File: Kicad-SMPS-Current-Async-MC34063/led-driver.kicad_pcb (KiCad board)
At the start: 2 copper layers, 40 x 25 mm, 16 parts, among them J1 Input 12V-30V, J2 Output, U1 MC34063, U2 LM321

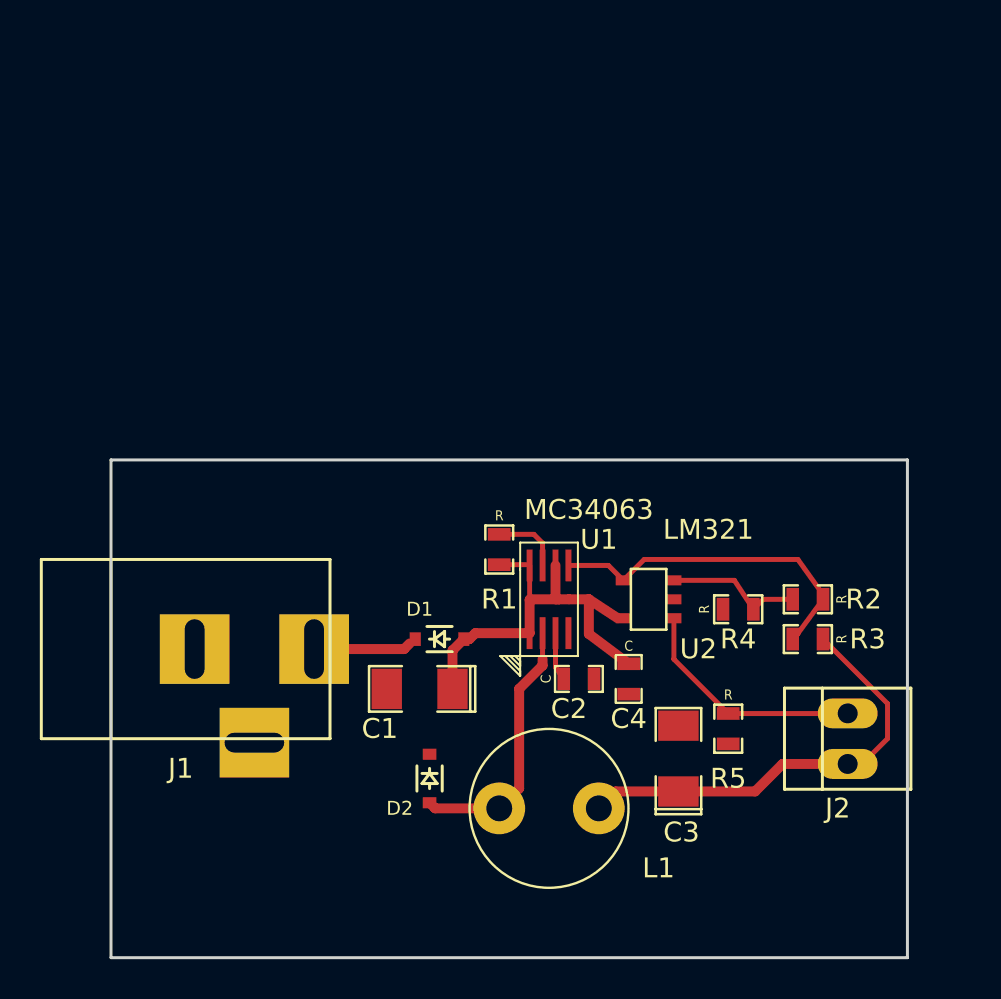
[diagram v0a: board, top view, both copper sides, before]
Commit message: Rebuild PCB to correct errors and generate group of eight circuits.
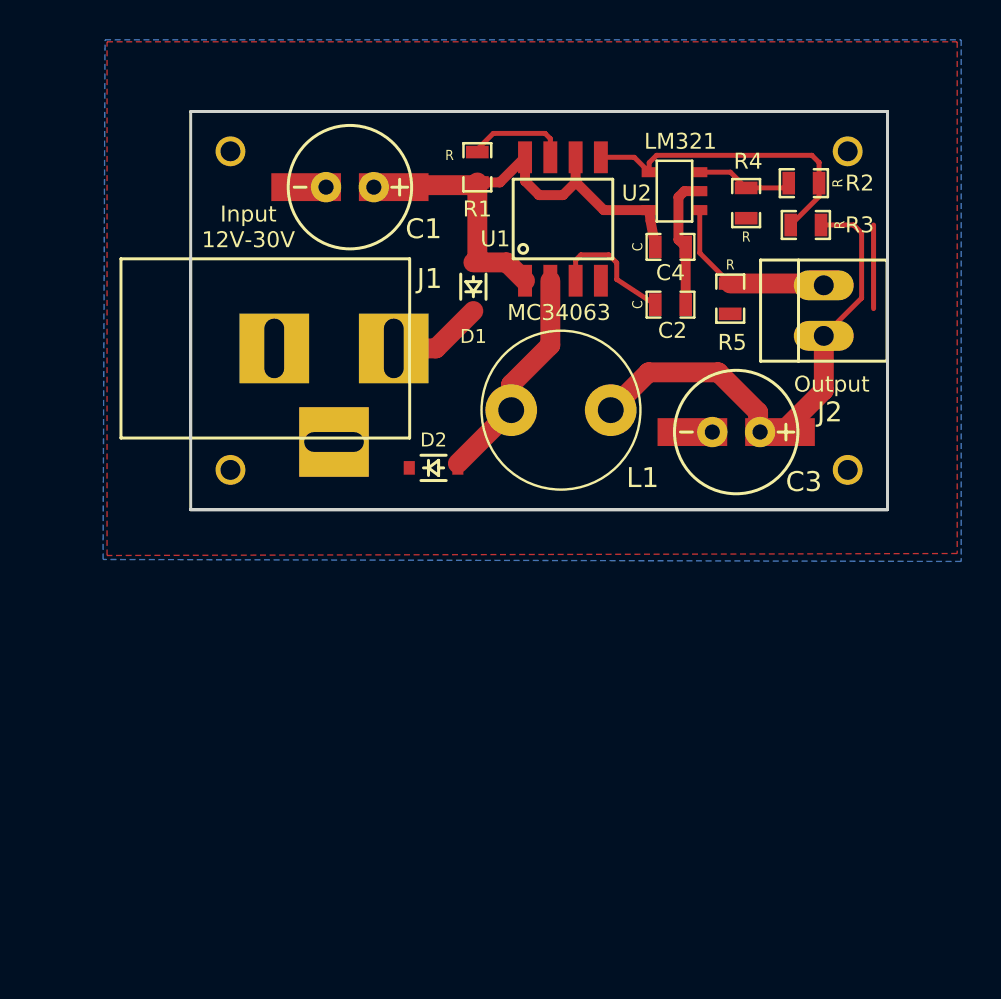
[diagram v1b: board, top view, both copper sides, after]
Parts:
- added J3: Conn_01x01, smps-current-source:THROUGHVIA, F.Cu at (157.0, 109.5)
- added J3: Conn_01x01, smps-current-source:THROUGHVIA, F.Cu at (126.0, 109.5)
- added J3: Conn_01x01, smps-current-source:THROUGHVIA, F.Cu at (126.0, 125.5)
- added J3: Conn_01x01, smps-current-source:THROUGHVIA, F.Cu at (157.0, 125.5)
- C1, C3: footprint smps-current-source:SM1206POL -> smps-current-source:RADIAL_TABBED_2.5mm_6.3mm
- U1: footprint smps-current-source:DCT(R-PDSO-G8) -> smps-current-source:SOIC_08_4.0mm_5.0mm_1.27mm
- moved C1 25.4 mm to (132.0, 111.3), turned to 0 degrees
- moved C4 21.8 mm to (148.1, 114.3), turned to 0 degrees
- moved R5 21.6 mm to (151.1, 116.9)
- moved J2 21.5 mm to (155.8, 117.5)
- moved R2 20.9 mm to (154.8, 111.1)
- moved R3 20.8 mm to (154.9, 113.2)
- moved U2 20.5 mm to (148.3, 111.5)
- moved R4 20.4 mm to (151.9, 112.1), turned to 90 degrees
- moved L1 20.0 mm to (140.1, 122.5)
- moved C2 19.4 mm to (148.1, 117.2)
- moved R1 19.2 mm to (138.4, 110.3)
- moved U1 19.1 mm to (142.7, 112.9)
- moved D1 17.8 mm to (138.2, 116.3), turned to 270 degrees
- moved C3 16.7 mm to (151.4, 123.6), turned to 0 degrees
- moved J1 15.6 mm to (128.0, 119.4)
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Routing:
- net Earth: track 0.00 -> 6.74 mm
- net /Vcc: track 22.2 -> 27.1 mm
- net (no net): track 0.00 -> 4.20 mm
- net Net-(C2-Pad1): track 2.43 -> 6.52 mm
- net Net-(C3-Pad1): track 21.8 -> 25.5 mm
- net Net-(J2-Pad2): track 11.9 -> 9.06 mm
- net Net-(D2-Pad1): track 13.6 -> 11.3 mm
- net Net-(R2-Pad2): track 6.96 -> 4.89 mm
- net Net-(R1-Pad1): track 3.48 -> 5.18 mm
- net Net-(R2-Pad1): track 17.0 -> 15.8 mm
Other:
- board size 40 x 25 mm -> 35 x 20 mm
- board text added: "Input 12V-30V"
- board text added: "Output"

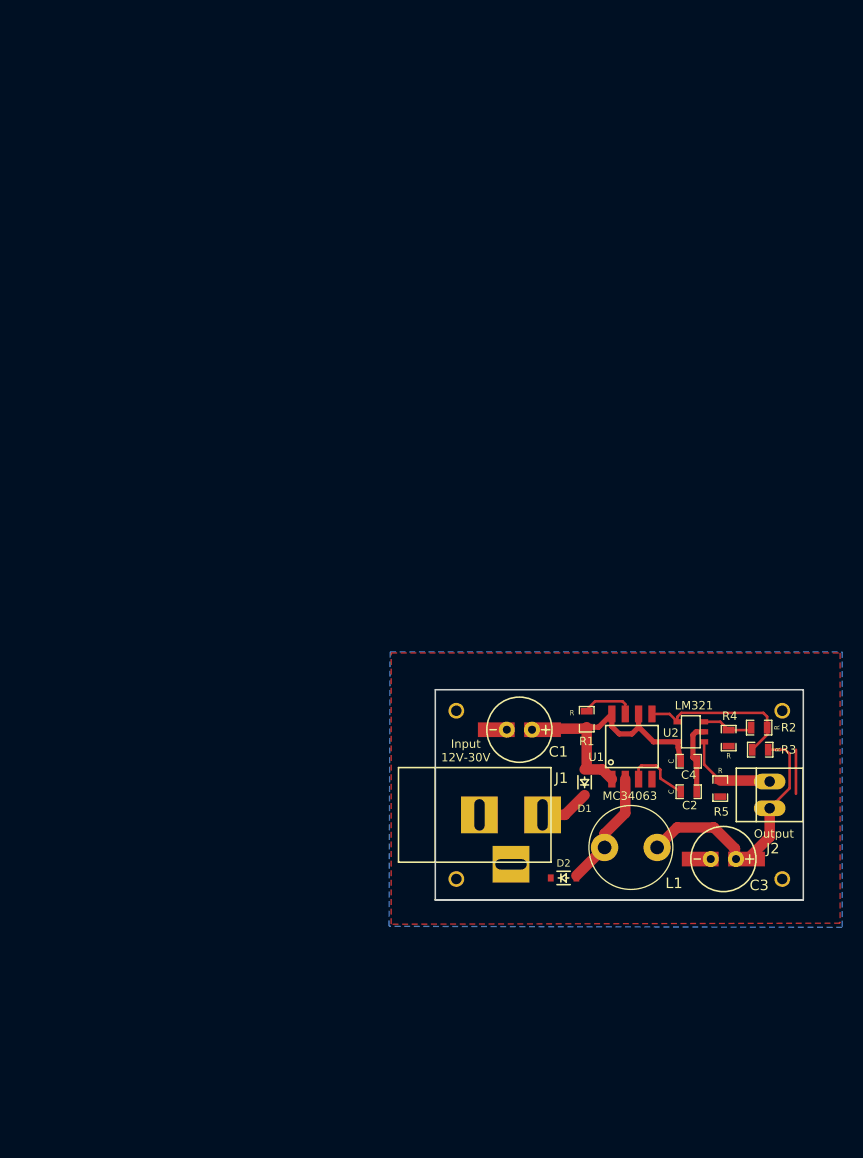
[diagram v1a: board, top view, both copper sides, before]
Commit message: Update PCB to make all sub-boards identical. Remove overhang on silk screen part of Barrel-Jack footprint.
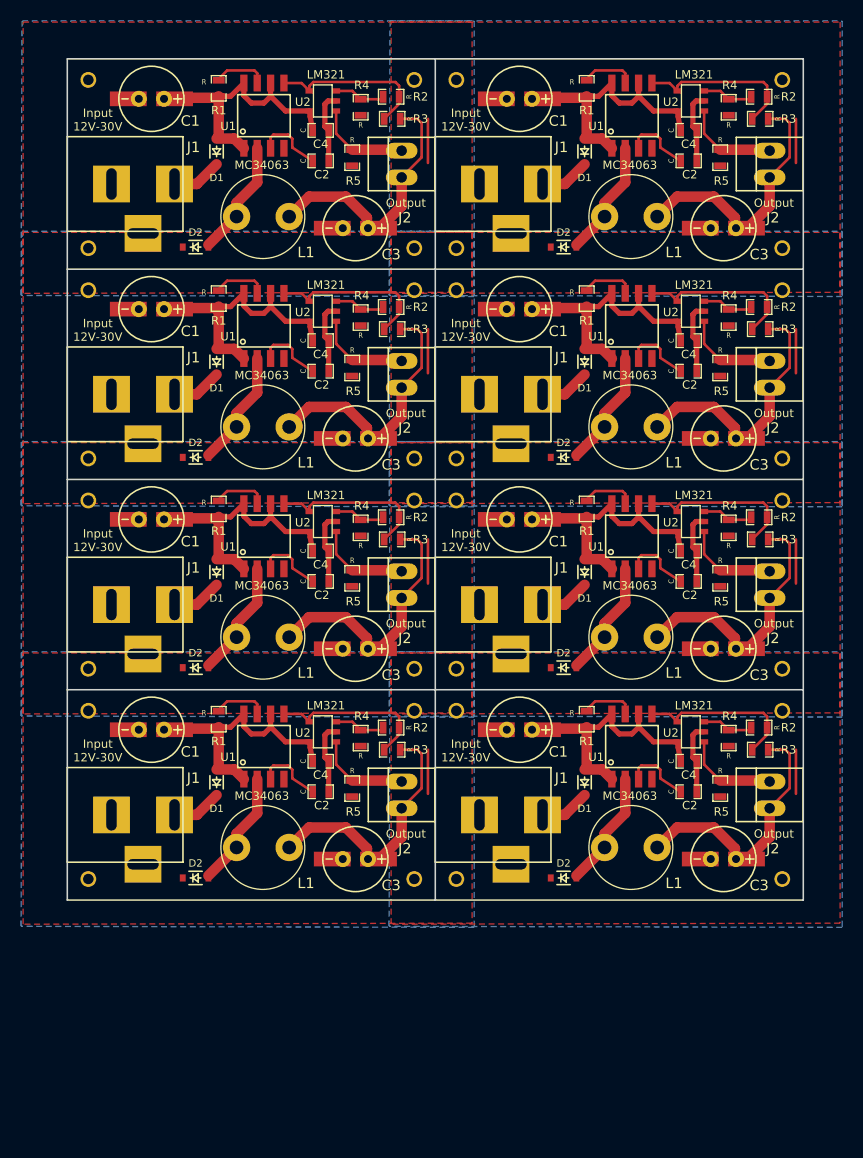
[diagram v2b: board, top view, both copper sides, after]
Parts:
- added C1: CP, smps-current-source:RADIAL_TABBED_2.5mm_6.3mm, F.Cu at (97.0, 111.3)
- added C1: CP, smps-current-source:RADIAL_TABBED_2.5mm_6.3mm, F.Cu at (97.0, 91.3)
- added C1: CP, smps-current-source:RADIAL_TABBED_2.5mm_6.3mm, F.Cu at (97.0, 51.3)
- added C1: CP, smps-current-source:RADIAL_TABBED_2.5mm_6.3mm, F.Cu at (97.0, 71.3)
- added C1: CP, smps-current-source:RADIAL_TABBED_2.5mm_6.3mm, F.Cu at (132.0, 71.3)
- added C1: CP, smps-current-source:RADIAL_TABBED_2.5mm_6.3mm, F.Cu at (132.0, 51.3)
- added C1: CP, smps-current-source:RADIAL_TABBED_2.5mm_6.3mm, F.Cu at (132.0, 91.3)
- added C2: C, smps-current-source:SM0603_Capa, F.Cu at (113.1, 117.2)
- added C2: C, smps-current-source:SM0603_Capa, F.Cu at (113.1, 97.2)
- added C2: C, smps-current-source:SM0603_Capa, F.Cu at (113.1, 57.2)
- added C2: C, smps-current-source:SM0603_Capa, F.Cu at (113.1, 77.2)
- added C2: C, smps-current-source:SM0603_Capa, F.Cu at (148.1, 77.2)
- added C2: C, smps-current-source:SM0603_Capa, F.Cu at (148.1, 57.2)
- added C2: C, smps-current-source:SM0603_Capa, F.Cu at (148.1, 97.2)
- added C3: CP, smps-current-source:RADIAL_TABBED_2.5mm_6.3mm, F.Cu at (116.4, 123.6)
- added C3: CP, smps-current-source:RADIAL_TABBED_2.5mm_6.3mm, F.Cu at (116.4, 103.6)
- added C3: CP, smps-current-source:RADIAL_TABBED_2.5mm_6.3mm, F.Cu at (116.4, 63.6)
- added C3: CP, smps-current-source:RADIAL_TABBED_2.5mm_6.3mm, F.Cu at (116.4, 83.6)
- added C3: CP, smps-current-source:RADIAL_TABBED_2.5mm_6.3mm, F.Cu at (151.4, 83.6)
- added C3: CP, smps-current-source:RADIAL_TABBED_2.5mm_6.3mm, F.Cu at (151.4, 63.6)
- added C3: CP, smps-current-source:RADIAL_TABBED_2.5mm_6.3mm, F.Cu at (151.4, 103.6)
- added C4: C, smps-current-source:SM0603_Capa, F.Cu at (113.1, 114.3)
- added C4: C, smps-current-source:SM0603_Capa, F.Cu at (113.1, 94.3)
- added C4: C, smps-current-source:SM0603_Capa, F.Cu at (113.1, 54.3)
- added C4: C, smps-current-source:SM0603_Capa, F.Cu at (113.1, 74.3)
- added C4: C, smps-current-source:SM0603_Capa, F.Cu at (148.1, 74.3)
- added C4: C, smps-current-source:SM0603_Capa, F.Cu at (148.1, 54.3)
- added C4: C, smps-current-source:SM0603_Capa, F.Cu at (148.1, 94.3)
- added D1: CUS15S30, smps-current-source:SOD-323, F.Cu at (103.2, 116.3)
- added D1: CUS15S30, smps-current-source:SOD-323, F.Cu at (103.2, 96.3)
- added D1: CUS15S30, smps-current-source:SOD-323, F.Cu at (103.2, 56.3)
- added D1: CUS15S30, smps-current-source:SOD-323, F.Cu at (103.2, 76.3)
- added D1: CUS15S30, smps-current-source:SOD-323, F.Cu at (138.2, 76.3)
- added D1: CUS15S30, smps-current-source:SOD-323, F.Cu at (138.2, 56.3)
- added D1: CUS15S30, smps-current-source:SOD-323, F.Cu at (138.2, 96.3)
- added D2: CUS15S30, smps-current-source:SOD-323, F.Cu at (101.2, 125.4)
- added D2: CUS15S30, smps-current-source:SOD-323, F.Cu at (101.2, 105.4)
- added D2: CUS15S30, smps-current-source:SOD-323, F.Cu at (101.2, 65.4)
- added D2: CUS15S30, smps-current-source:SOD-323, F.Cu at (101.2, 85.4)
- added D2: CUS15S30, smps-current-source:SOD-323, F.Cu at (136.2, 85.4)
- added D2: CUS15S30, smps-current-source:SOD-323, F.Cu at (136.2, 65.4)
- added D2: CUS15S30, smps-current-source:SOD-323, F.Cu at (136.2, 105.4)
- added J1: Input 12V-30V, smps-current-source:BARREL_JACK, F.Cu at (93.0, 119.4)
- added J1: Input 12V-30V, smps-current-source:BARREL_JACK, F.Cu at (93.0, 99.4)
- added J1: Input 12V-30V, smps-current-source:BARREL_JACK, F.Cu at (93.0, 59.4)
- added J1: Input 12V-30V, smps-current-source:BARREL_JACK, F.Cu at (93.0, 79.4)
- added J1: Input 12V-30V, smps-current-source:BARREL_JACK, F.Cu at (128.0, 79.4)
- added J1: Input 12V-30V, smps-current-source:BARREL_JACK, F.Cu at (128.0, 59.4)
- added J1: Input 12V-30V, smps-current-source:BARREL_JACK, F.Cu at (128.0, 99.4)
- added J2: Output, smps-current-source:PINHEAD1-2, F.Cu at (120.8, 117.5)
- added J2: Output, smps-current-source:PINHEAD1-2, F.Cu at (120.8, 97.5)
- added J2: Output, smps-current-source:PINHEAD1-2, F.Cu at (120.8, 57.5)
- added J2: Output, smps-current-source:PINHEAD1-2, F.Cu at (120.8, 77.5)
- added J2: Output, smps-current-source:PINHEAD1-2, F.Cu at (155.8, 77.5)
- added J2: Output, smps-current-source:PINHEAD1-2, F.Cu at (155.8, 57.5)
- added J2: Output, smps-current-source:PINHEAD1-2, F.Cu at (155.8, 97.5)
- added J3: Conn_01x01, smps-current-source:THROUGHVIA, F.Cu at (122.0, 125.5)
- added J3: Conn_01x01, smps-current-source:THROUGHVIA, F.Cu at (91.0, 65.5)
- added J3: Conn_01x01, smps-current-source:THROUGHVIA, F.Cu at (91.0, 49.5)
- added J3: Conn_01x01, smps-current-source:THROUGHVIA, F.Cu at (122.0, 49.5)
- added J3: Conn_01x01, smps-current-source:THROUGHVIA, F.Cu at (122.0, 69.5)
- added J3: Conn_01x01, smps-current-source:THROUGHVIA, F.Cu at (91.0, 69.5)
- added J3: Conn_01x01, smps-current-source:THROUGHVIA, F.Cu at (91.0, 85.5)
- added J3: Conn_01x01, smps-current-source:THROUGHVIA, F.Cu at (122.0, 85.5)
- added J3: Conn_01x01, smps-current-source:THROUGHVIA, F.Cu at (157.0, 85.5)
- added J3: Conn_01x01, smps-current-source:THROUGHVIA, F.Cu at (126.0, 85.5)
- added J3: Conn_01x01, smps-current-source:THROUGHVIA, F.Cu at (126.0, 69.5)
- added J3: Conn_01x01, smps-current-source:THROUGHVIA, F.Cu at (91.0, 125.5)
- added J3: Conn_01x01, smps-current-source:THROUGHVIA, F.Cu at (157.0, 69.5)
- added J3: Conn_01x01, smps-current-source:THROUGHVIA, F.Cu at (157.0, 49.5)
- added J3: Conn_01x01, smps-current-source:THROUGHVIA, F.Cu at (126.0, 49.5)
- added J3: Conn_01x01, smps-current-source:THROUGHVIA, F.Cu at (126.0, 65.5)
- added J3: Conn_01x01, smps-current-source:THROUGHVIA, F.Cu at (157.0, 65.5)
- added J3: Conn_01x01, smps-current-source:THROUGHVIA, F.Cu at (157.0, 105.5)
- added J3: Conn_01x01, smps-current-source:THROUGHVIA, F.Cu at (126.0, 105.5)
- added J3: Conn_01x01, smps-current-source:THROUGHVIA, F.Cu at (126.0, 89.5)
- added J3: Conn_01x01, smps-current-source:THROUGHVIA, F.Cu at (157.0, 89.5)
- added J3: Conn_01x01, smps-current-source:THROUGHVIA, F.Cu at (91.0, 109.5)
- added J3: Conn_01x01, smps-current-source:THROUGHVIA, F.Cu at (122.0, 109.5)
- added J3: Conn_01x01, smps-current-source:THROUGHVIA, F.Cu at (122.0, 89.5)
- added J3: Conn_01x01, smps-current-source:THROUGHVIA, F.Cu at (91.0, 89.5)
- added J3: Conn_01x01, smps-current-source:THROUGHVIA, F.Cu at (91.0, 105.5)
- added J3: Conn_01x01, smps-current-source:THROUGHVIA, F.Cu at (122.0, 105.5)
- added J3: Conn_01x01, smps-current-source:THROUGHVIA, F.Cu at (122.0, 65.5)
- added L1: L, smps-current-source:L_Radial_D7.8mm_P5.00mm_Fastron_07HCP, F.Cu at (105.1, 122.5)
- added L1: L, smps-current-source:L_Radial_D7.8mm_P5.00mm_Fastron_07HCP, F.Cu at (105.1, 102.5)
- added L1: L, smps-current-source:L_Radial_D7.8mm_P5.00mm_Fastron_07HCP, F.Cu at (105.1, 62.5)
- added L1: L, smps-current-source:L_Radial_D7.8mm_P5.00mm_Fastron_07HCP, F.Cu at (105.1, 82.5)
- added L1: L, smps-current-source:L_Radial_D7.8mm_P5.00mm_Fastron_07HCP, F.Cu at (140.1, 82.5)
- added L1: L, smps-current-source:L_Radial_D7.8mm_P5.00mm_Fastron_07HCP, F.Cu at (140.1, 62.5)
- added L1: L, smps-current-source:L_Radial_D7.8mm_P5.00mm_Fastron_07HCP, F.Cu at (140.1, 102.5)
- added R1: R, smps-current-source:SM0603_Resistor, F.Cu at (103.4, 110.3)
- added R1: R, smps-current-source:SM0603_Resistor, F.Cu at (103.4, 90.3)
- added R1: R, smps-current-source:SM0603_Resistor, F.Cu at (103.4, 50.3)
- added R1: R, smps-current-source:SM0603_Resistor, F.Cu at (103.4, 70.3)
- added R1: R, smps-current-source:SM0603_Resistor, F.Cu at (138.4, 70.3)
- added R1: R, smps-current-source:SM0603_Resistor, F.Cu at (138.4, 50.3)
- added R1: R, smps-current-source:SM0603_Resistor, F.Cu at (138.4, 90.3)
- added R2: R, smps-current-source:SM0603_Resistor, F.Cu at (119.8, 111.1)
- added R2: R, smps-current-source:SM0603_Resistor, F.Cu at (119.8, 91.1)
- added R2: R, smps-current-source:SM0603_Resistor, F.Cu at (119.8, 51.1)
- added R2: R, smps-current-source:SM0603_Resistor, F.Cu at (119.8, 71.1)
- added R2: R, smps-current-source:SM0603_Resistor, F.Cu at (154.8, 71.1)
- added R2: R, smps-current-source:SM0603_Resistor, F.Cu at (154.8, 51.1)
- added R2: R, smps-current-source:SM0603_Resistor, F.Cu at (154.8, 91.1)
- added R3: R, smps-current-source:SM0603_Resistor, F.Cu at (119.9, 113.2)
- added R3: R, smps-current-source:SM0603_Resistor, F.Cu at (119.9, 93.2)
- added R3: R, smps-current-source:SM0603_Resistor, F.Cu at (119.9, 53.2)
- added R3: R, smps-current-source:SM0603_Resistor, F.Cu at (119.9, 73.2)
- added R3: R, smps-current-source:SM0603_Resistor, F.Cu at (154.9, 73.2)
- added R3: R, smps-current-source:SM0603_Resistor, F.Cu at (154.9, 53.2)
- added R3: R, smps-current-source:SM0603_Resistor, F.Cu at (154.9, 93.2)
- added R4: R, smps-current-source:SM0603_Resistor, F.Cu at (116.9, 112.1)
- added R4: R, smps-current-source:SM0603_Resistor, F.Cu at (116.9, 92.1)
- added R4: R, smps-current-source:SM0603_Resistor, F.Cu at (116.9, 52.1)
- added R4: R, smps-current-source:SM0603_Resistor, F.Cu at (116.9, 72.1)
- added R4: R, smps-current-source:SM0603_Resistor, F.Cu at (151.9, 72.1)
- added R4: R, smps-current-source:SM0603_Resistor, F.Cu at (151.9, 52.1)
- added R4: R, smps-current-source:SM0603_Resistor, F.Cu at (151.9, 92.1)
- added R5: R, smps-current-source:SM0603_Resistor, F.Cu at (116.1, 116.9)
- added R5: R, smps-current-source:SM0603_Resistor, F.Cu at (116.1, 96.9)
- added R5: R, smps-current-source:SM0603_Resistor, F.Cu at (116.1, 56.9)
- added R5: R, smps-current-source:SM0603_Resistor, F.Cu at (116.1, 76.9)
- added R5: R, smps-current-source:SM0603_Resistor, F.Cu at (151.1, 76.9)
- added R5: R, smps-current-source:SM0603_Resistor, F.Cu at (151.1, 56.9)
- added R5: R, smps-current-source:SM0603_Resistor, F.Cu at (151.1, 96.9)
- added U1: MC34063, smps-current-source:SOIC_08_4.0mm_5.0mm_1.27mm, F.Cu at (107.7, 112.9)
- added U1: MC34063, smps-current-source:SOIC_08_4.0mm_5.0mm_1.27mm, F.Cu at (107.7, 92.9)
- added U1: MC34063, smps-current-source:SOIC_08_4.0mm_5.0mm_1.27mm, F.Cu at (107.7, 52.9)
- added U1: MC34063, smps-current-source:SOIC_08_4.0mm_5.0mm_1.27mm, F.Cu at (107.7, 72.9)
- added U1: MC34063, smps-current-source:SOIC_08_4.0mm_5.0mm_1.27mm, F.Cu at (142.7, 72.9)
- added U1: MC34063, smps-current-source:SOIC_08_4.0mm_5.0mm_1.27mm, F.Cu at (142.7, 52.9)
- added U1: MC34063, smps-current-source:SOIC_08_4.0mm_5.0mm_1.27mm, F.Cu at (142.7, 92.9)
- added U2: LM321, smps-current-source:SOT23-5, F.Cu at (113.3, 111.5)
- added U2: LM321, smps-current-source:SOT23-5, F.Cu at (113.3, 91.5)
- added U2: LM321, smps-current-source:SOT23-5, F.Cu at (113.3, 51.5)
- added U2: LM321, smps-current-source:SOT23-5, F.Cu at (113.3, 71.5)
- added U2: LM321, smps-current-source:SOT23-5, F.Cu at (148.3, 71.5)
- added U2: LM321, smps-current-source:SOT23-5, F.Cu at (148.3, 51.5)
- added U2: LM321, smps-current-source:SOT23-5, F.Cu at (148.3, 91.5)
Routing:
- net /Vcc: track 27.1 -> 216.4 mm
- net Net-(C3-Pad1): track 25.5 -> 204.2 mm
- net Net-(R2-Pad1): track 15.8 -> 126.2 mm
- net Net-(D2-Pad1): track 11.3 -> 90.6 mm
- net Net-(J2-Pad2): track 9.06 -> 72.5 mm
- net Earth: track 6.74 -> 54.0 mm
- net Net-(C2-Pad1): track 6.52 -> 52.2 mm
- net Net-(R1-Pad1): track 5.18 -> 41.4 mm
- net Net-(R2-Pad2): track 4.89 -> 39.2 mm
- net Net-(D1-Pad2): track 4.78 -> 38.2 mm
- net (no net): track 4.20 -> 33.6 mm
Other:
- board size 35 x 20 mm -> 70 x 80 mm

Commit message: Fix problem with current limiting resistor and also silk screen of diodes.
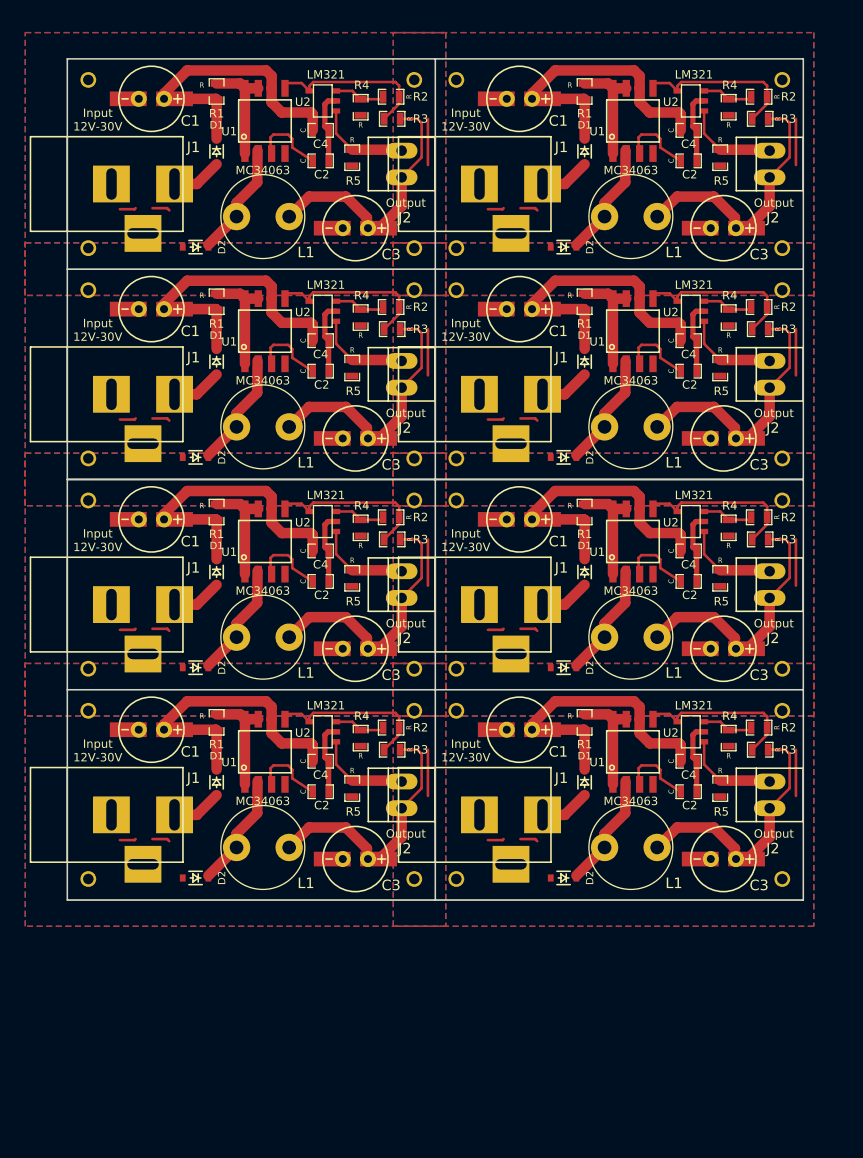
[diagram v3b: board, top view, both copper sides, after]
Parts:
- removed the R1 at (103.4, 110.3)
- removed the R1 at (103.4, 90.3)
- removed the R1 at (103.4, 50.3)
- removed the R1 at (103.4, 70.3)
- removed the R1 at (138.4, 70.3)
- removed the R1 at (138.4, 50.3)
- removed the R1 at (138.4, 90.3)
- removed the U1 at (107.7, 112.9)
- removed the U1 at (107.7, 92.9)
- removed the U1 at (107.7, 52.9)
- removed the U1 at (107.7, 72.9)
- removed the U1 at (142.7, 72.9)
- removed the U1 at (142.7, 52.9)
- removed the U1 at (142.7, 92.9)
- added R1: R, smps-current-source:SM0603_Resistor, F.Cu at (138.2, 70.6)
- added R1: R, smps-current-source:SM0603_Resistor, F.Cu at (138.2, 50.6)
- added R1: R, smps-current-source:SM0603_Resistor, F.Cu at (103.2, 50.6)
- added R1: R, smps-current-source:SM0603_Resistor, F.Cu at (103.2, 70.6)
- added R1: R, smps-current-source:SM0603_Resistor, F.Cu at (103.2, 110.6)
- added R1: R, smps-current-source:SM0603_Resistor, F.Cu at (103.2, 90.6)
- added R1: R, smps-current-source:SM0603_Resistor, F.Cu at (138.2, 90.6)
- added U1: MC34063, smps-current-source:SOIC_08_4.0mm_5.0mm_1.27mm, F.Cu at (142.8, 73.4)
- added U1: MC34063, smps-current-source:SOIC_08_4.0mm_5.0mm_1.27mm, F.Cu at (142.8, 53.4)
- added U1: MC34063, smps-current-source:SOIC_08_4.0mm_5.0mm_1.27mm, F.Cu at (107.8, 53.4)
- added U1: MC34063, smps-current-source:SOIC_08_4.0mm_5.0mm_1.27mm, F.Cu at (107.8, 73.4)
- added U1: MC34063, smps-current-source:SOIC_08_4.0mm_5.0mm_1.27mm, F.Cu at (107.8, 113.4)
- added U1: MC34063, smps-current-source:SOIC_08_4.0mm_5.0mm_1.27mm, F.Cu at (107.8, 93.4)
- added U1: MC34063, smps-current-source:SOIC_08_4.0mm_5.0mm_1.27mm, F.Cu at (142.8, 93.4)
- moved U1 0.51 mm to (142.8, 113.4)
- moved R1 0.36 mm to (138.2, 110.6)
- turned D1 to 90 degrees (x8)
- turned D2 to 0 degrees (x5)
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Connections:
- U1 pad 1: /Vcc -> Net-(R1-Pad1)
- U1 pad 8: /Vcc -> Net-(R1-Pad1)
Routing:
- net Net-(R1-Pad1): track 41.4 -> 82.9 mm
- net (no net): track 33.6 -> 61.0 mm
- net /Vcc: track 216.4 -> 232.2 mm
- net Net-(D2-Pad1): track 90.6 -> 89.0 mm
